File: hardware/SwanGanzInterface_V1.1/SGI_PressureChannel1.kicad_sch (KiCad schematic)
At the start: 18 parts, among them J5 Conn_01x04_Pin, U10 INA122D, U11 OPA2350

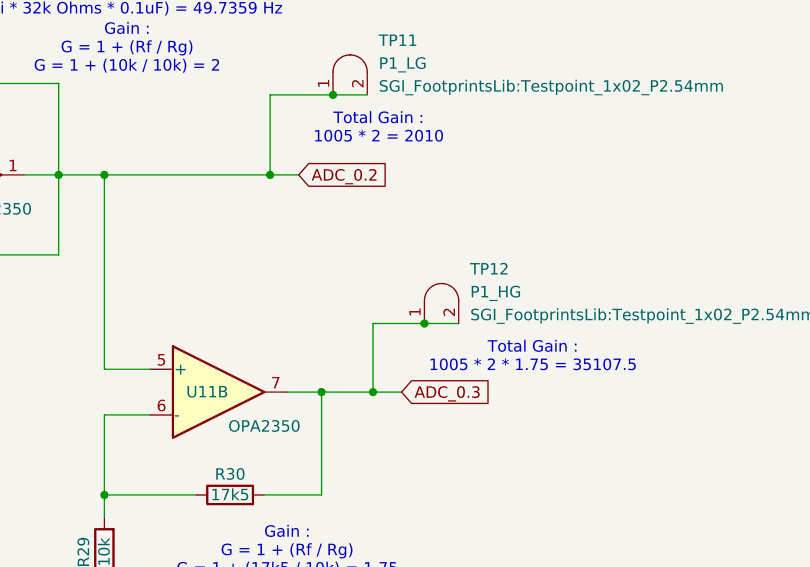
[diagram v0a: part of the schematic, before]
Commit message: Pin Allocation, updated schematic with new pins, reassigned
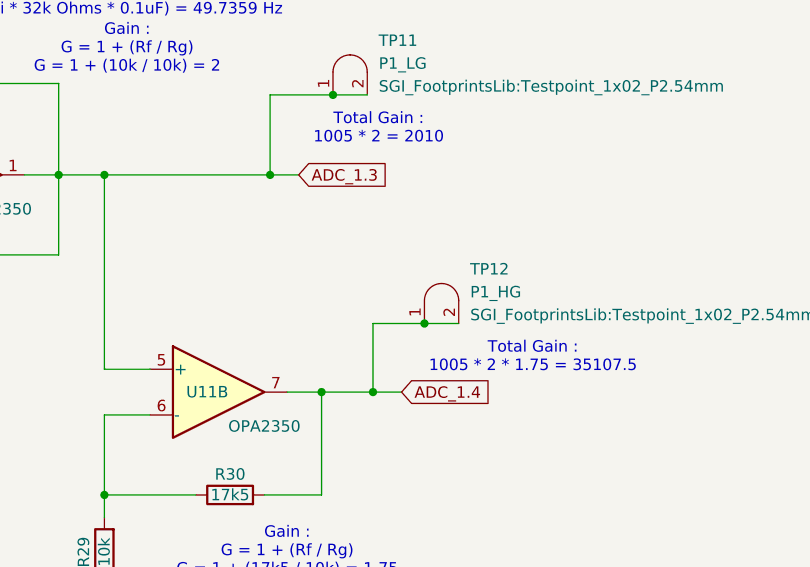
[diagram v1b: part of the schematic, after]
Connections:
- net ADC_0.2 renamed ADC_1.3
- net ADC_0.3 renamed ADC_1.4
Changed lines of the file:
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@@
 		)
 	)
-	(global_label "ADC_0.3"
+	(global_label "ADC_1.4"
 		(shape input)
 		(at 179.07 88.9 0)
@@
 		)
 	)
-	(global_label "ADC_0.2"
+	(global_label "ADC_1.3"
 		(shape input)
 		(at 167.64 64.77 0)

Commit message: Hooked up MSP
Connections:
- net ADC_1.3 renamed P1_LG_ADC_1.3
- net ADC_1.4 renamed P1_HG_ADC_1.4
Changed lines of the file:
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@@
 		)
 	)
-	(global_label "ADC_1.4"
+	(global_label "P1_HG_ADC_1.4"
 		(shape input)
 		(at 179.07 88.9 0)
@@
 		)
 		(property "Intersheetrefs" "${INTERSHEET_REFS}"
-			(at 189.6752 88.9 0)
+			(at 196.6904 88.9 0)
 			(effects
 				(font
@@
 		)
 	)
-	(global_label "ADC_1.3"
+	(global_label "P1_LG_ADC_1.3"
 		(shape input)
 		(at 167.64 64.77 0)
@@
 		)
 		(property "Intersheetrefs" "${INTERSHEET_REFS}"
-			(at 178.2452 64.77 0)
+			(at 184.958 64.77 0)
 			(effects
 				(font

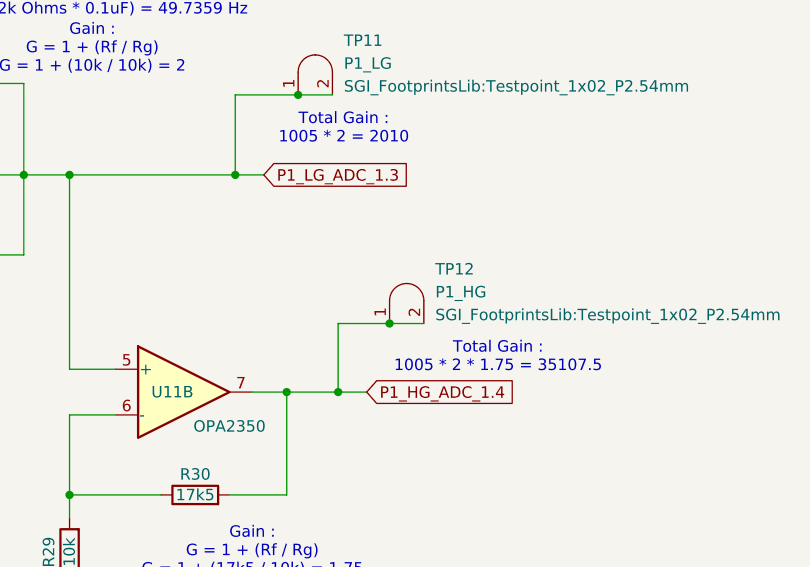
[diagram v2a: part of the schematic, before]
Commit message: Started converting things to use touch screen chip
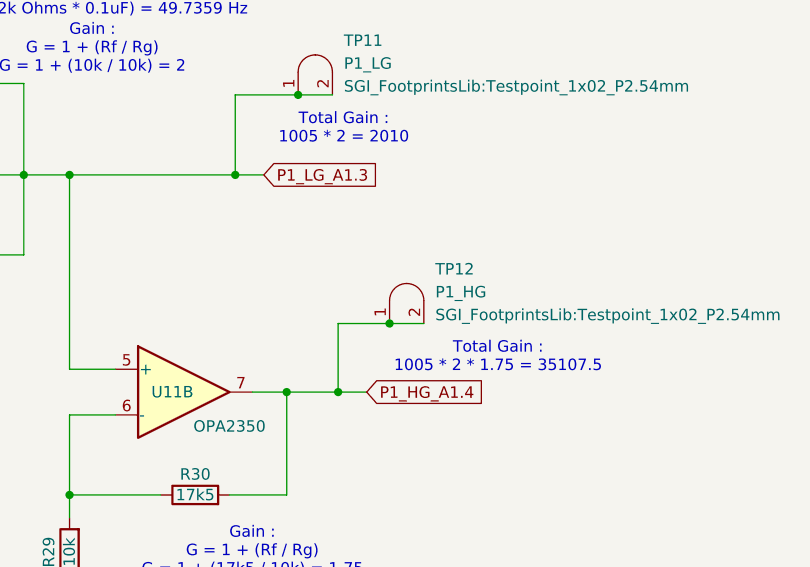
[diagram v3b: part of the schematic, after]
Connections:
- net P1_HG_ADC_1.4 renamed P1_HG_A1.4
- net P1_LG_ADC_1.3 renamed P1_LG_A1.3
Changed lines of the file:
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@@
 		)
 	)
-	(global_label "P1_HG_ADC_1.4"
+	(global_label "P1_HG_A1.4"
 		(shape input)
 		(at 179.07 88.9 0)
@@
 		)
 		(property "Intersheetrefs" "${INTERSHEET_REFS}"
-			(at 196.6904 88.9 0)
+			(at 193.1828 88.9 0)
 			(effects
 				(font
@@
 		)
 	)
-	(global_label "P1_LG_ADC_1.3"
+	(global_label "P1_LG_A1.3"
 		(shape input)
 		(at 167.64 64.77 0)
@@
 		)
 		(property "Intersheetrefs" "${INTERSHEET_REFS}"
-			(at 184.958 64.77 0)
+			(at 181.4504 64.77 0)
 			(effects
 				(font

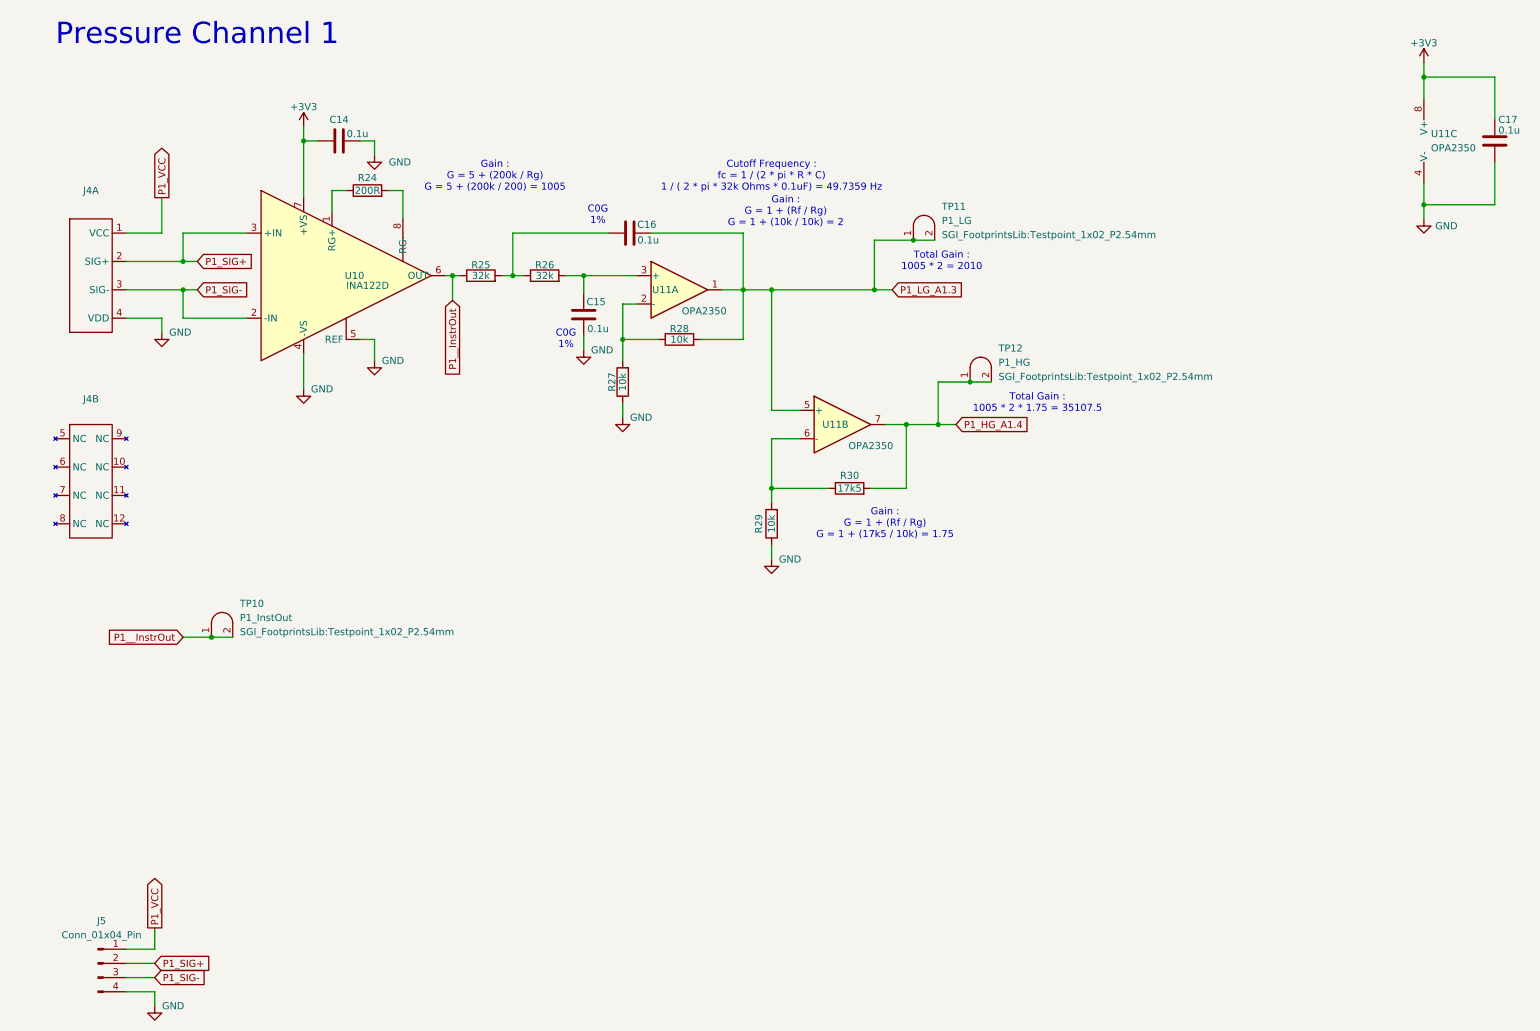
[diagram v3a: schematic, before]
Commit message: Got 64 pin MSP symbol and footprint and started implementation
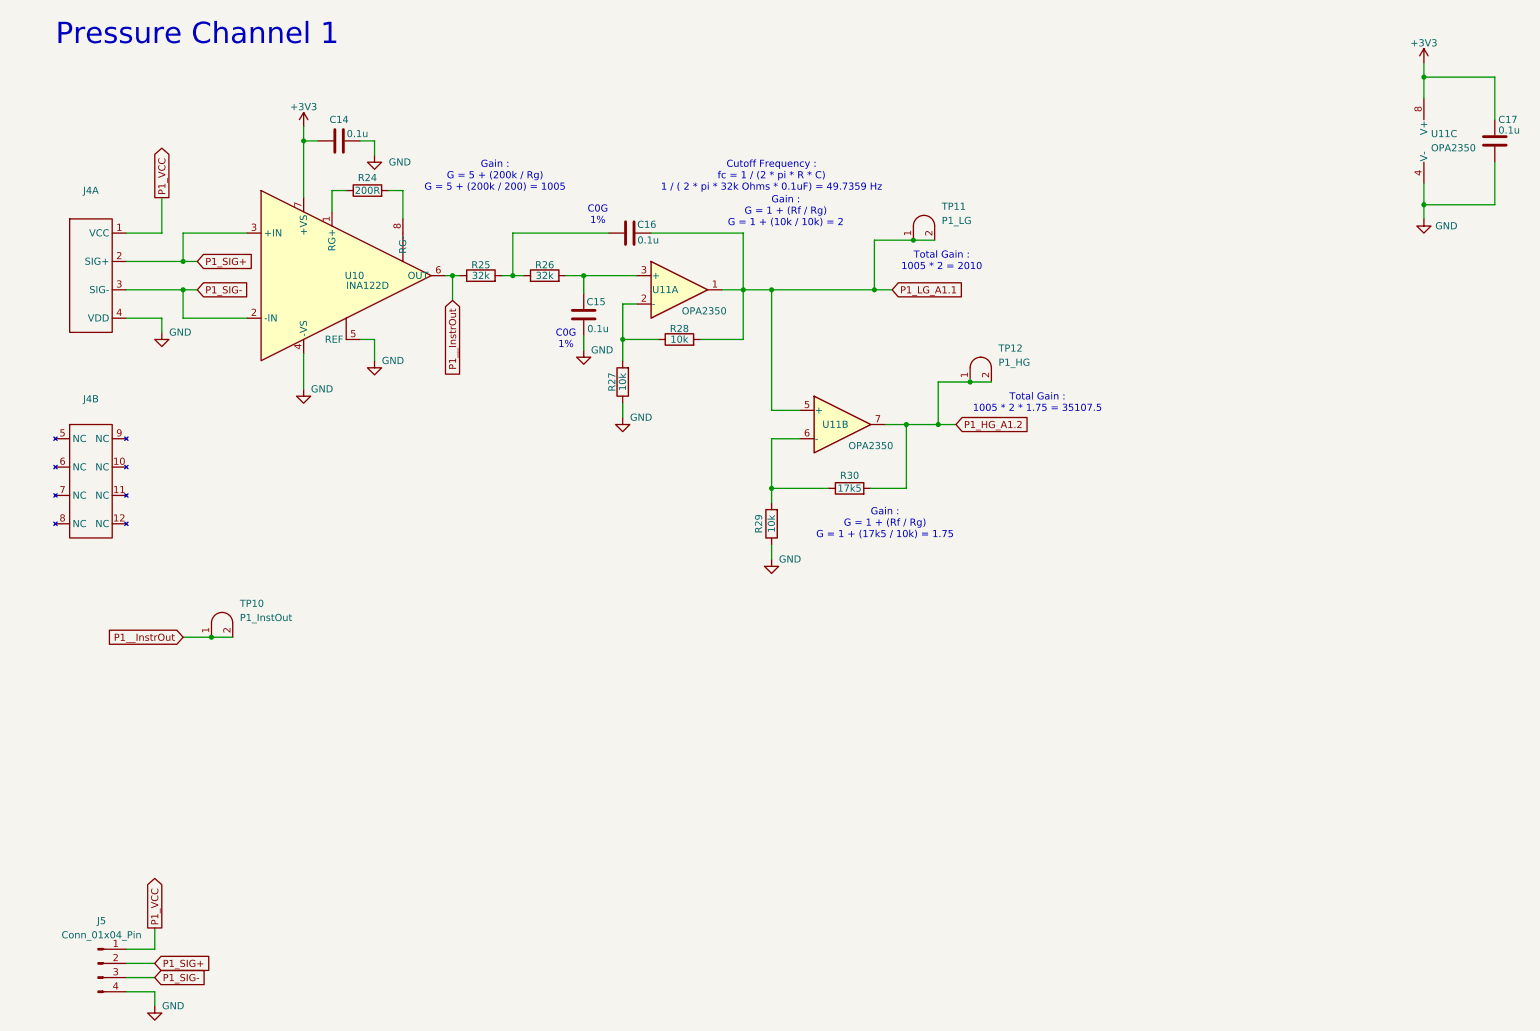
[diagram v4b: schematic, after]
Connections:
- net P1_HG_A1.4 renamed P1_HG_A1.2
- net P1_LG_A1.3 renamed P1_LG_A1.1
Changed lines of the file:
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@@
 		)
 	)
-	(global_label "P1_HG_A1.4"
+	(global_label "P1_HG_A1.2"
 		(shape input)
 		(at 179.07 88.9 0)
@@
 		)
 	)
-	(global_label "P1_LG_A1.3"
+	(global_label "P1_LG_A1.1"
 		(shape input)
 		(at 167.64 64.77 0)
@@
 				)
 				(justify left)
+				(hide yes)
 			)
 		)
@@
 				)
 				(justify left)
+				(hide yes)
 			)
 		)
@@
 				)
 				(justify left)
-			)
-		)
+				(hide yes)
+			)
+		)

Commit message: Schematic Check
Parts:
- renumbered C14 to C19, C15 to C20, C16 to C21, C17 to C22, R24 to R22, R25 to R23, R26 to R24, R27 to R25, R28 to R26, R29 to R27, R30 to R28, U10 to U7, U11 to U8
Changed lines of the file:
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@@
 		(on_board yes)
 		(dnp no)
-		(property "Reference" "#PWR056"
+		(property "Reference" "#PWR054"
 			(at 146.05 119.38 0)
 			(effects
@@
 			(project "SwanGanzInterface"
 				(path "/4e9a6e30-f660-472b-9696-bea1f34b4545/3d8fa9e7-4833-4941-a955-d778effe3e32"
-					(reference "#PWR056")
+					(reference "#PWR054")
 					(unit 1)
 				)
@@
 		(dnp no)
 		(fields_autoplaced yes)
-		(property "Reference" "#PWR052"
+		(property "Reference" "#PWR050"
 			(at 74.93 46.99 0)
 			(effects
@@
 			(project "SwanGanzInterface"
 				(path "/4e9a6e30-f660-472b-9696-bea1f34b4545/3d8fa9e7-4833-4941-a955-d778effe3e32"
-					(reference "#PWR052")
+					(reference "#PWR050")
 					(unit 1)
 				)
@@
 		(on_board yes)
 		(dnp no)
-		(property "Reference" "R28"
+		(property "Reference" "R26"
 			(at 129.54 71.755 90)
 			(effects
@@
 			(project "SwanGanzInterface"
 				(path "/4e9a6e30-f660-472b-9696-bea1f34b4545/3d8fa9e7-4833-4941-a955-d778effe3e32"
-					(reference "R28")
+					(reference "R26")
 					(unit 1)
 				)
@@
 		(on_board yes)
 		(dnp no)
-		(property "Reference" "C15"
+		(property "Reference" "C20"
 			(at 112.903 66.929 0)
 			(effects
@@
 			(project "SwanGanzInterface"
 				(path "/4e9a6e30-f660-472b-9696-bea1f34b4545/3d8fa9e7-4833-4941-a955-d778effe3e32"
-					(reference "C15")
+					(reference "C20")
 					(unit 1)
 				)
@@
 		(on_board yes)
 		(dnp no)
-		(property "Reference" "#PWR054"
+		(property "Reference" "#PWR052"
 			(at 112.395 81.915 0)
 			(effects
@@
 			(project "SwanGanzInterface"
 				(path "/4e9a6e30-f660-472b-9696-bea1f34b4545/3d8fa9e7-4833-4941-a955-d778effe3e32"
-					(reference "#PWR054")
+					(reference "#PWR052")
 					(unit 1)
 				)
@@
 		(on_board yes)
 		(dnp no)
-		(property "Reference" "R26"
+		(property "Reference" "R24"
 			(at 105.41 60.325 90)
 			(effects
@@
 			(project "SwanGanzInterface"
 				(path "/4e9a6e30-f660-472b-9696-bea1f34b4545/3d8fa9e7-4833-4941-a955-d778effe3e32"
-					(reference "R26")
+					(reference "R24")
 					(unit 1)
 				)
@@
 		(on_board yes)
 		(dnp no)
-		(property "Reference" "U11"
+		(property "Reference" "U8"
 			(at 127 64.77 0)
 			(effects
@@
 			(project "SwanGanzInterface"
 				(path "/4e9a6e30-f660-472b-9696-bea1f34b4545/3d8fa9e7-4833-4941-a955-d778effe3e32"
-					(reference "U11")
+					(reference "U8")
 					(unit 1)
 				)
@@
 		(on_board yes)
 		(dnp no)
-		(property "Reference" "#PWR051"
+		(property "Reference" "#PWR049"
 			(at 62.23 88.9 0)
 			(effects
@@
 			(project "SwanGanzInterface"
 				(path "/4e9a6e30-f660-472b-9696-bea1f34b4545/3d8fa9e7-4833-4941-a955-d778effe3e32"
-					(reference "#PWR051")
+					(reference "#PWR049")
 					(unit 1)
 				)
@@
 		(on_board yes)
 		(dnp no)
-		(property "Reference" "#PWR048"
+		(property "Reference" "#PWR046"
 			(at 35.56 199.39 0)
 			(effects
@@
 			(project "SwanGanzInterface"
 				(path "/4e9a6e30-f660-472b-9696-bea1f34b4545/3d8fa9e7-4833-4941-a955-d778effe3e32"
-					(reference "#PWR048")
+					(reference "#PWR046")
 					(unit 1)
 				)
@@
 		(on_board yes)
 		(dnp no)
-		(property "Reference" "#PWR055"
+		(property "Reference" "#PWR053"
 			(at 119.38 93.98 0)
 			(effects
@@
 			(project "SwanGanzInterface"
 				(path "/4e9a6e30-f660-472b-9696-bea1f34b4545/3d8fa9e7-4833-4941-a955-d778effe3e32"
-					(reference "#PWR055")
+					(reference "#PWR053")
 					(unit 1)
 				)
@@
 		(dnp no)
 		(fields_autoplaced yes)
-		(property "Reference" "U11"
+		(property "Reference" "U8"
 			(at 264.16 36.8299 0)
 			(effects
@@
 			(project "SwanGanzInterface"
 				(path "/4e9a6e30-f660-472b-9696-bea1f34b4545/3d8fa9e7-4833-4941-a955-d778effe3e32"
-					(reference "U11")
+					(reference "U8")
 					(unit 3)
 				)
@@
 		(dnp no)
 		(fields_autoplaced yes)
-		(property "Reference" "#PWR058"
+		(property "Reference" "#PWR056"
 			(at 262.89 58.42 0)
 			(effects
@@
 			(project "SwanGanzInterface"
 				(path "/4e9a6e30-f660-472b-9696-bea1f34b4545/3d8fa9e7-4833-4941-a955-d778effe3e32"
-					(reference "#PWR058")
+					(reference "#PWR056")
 					(unit 1)
 				)
@@
 		(on_board yes)
 		(dnp no)
-		(property "Reference" "#PWR050"
+		(property "Reference" "#PWR048"
 			(at 62.23 39.37 0)
 			(effects
@@
 			(project "SwanGanzInterface"
 				(path "/4e9a6e30-f660-472b-9696-bea1f34b4545/3d8fa9e7-4833-4941-a955-d778effe3e32"
-					(reference "#PWR050")
+					(reference "#PWR048")
 					(unit 1)
 				)
@@
 		(on_board yes)
 		(dnp no)
-		(property "Reference" "R29"
+		(property "Reference" "R27"
 			(at 143.764 106.68 90)
 			(effects
@@
 			(project "SwanGanzInterface"
 				(path "/4e9a6e30-f660-472b-9696-bea1f34b4545/3d8fa9e7-4833-4941-a955-d778effe3e32"
-					(reference "R29")
+					(reference "R27")
 					(unit 1)
 				)
@@
 		(on_board yes)
 		(dnp no)
-		(property "Reference" "U11"
+		(property "Reference" "U8"
 			(at 157.48 88.9 0)
 			(effects
@@
 			(project "SwanGanzInterface"
 				(path "/4e9a6e30-f660-472b-9696-bea1f34b4545/3d8fa9e7-4833-4941-a955-d778effe3e32"
-					(reference "U11")
+					(reference "U8")
 					(unit 2)
 				)
@@
 		(on_board yes)
 		(dnp no)
-		(property "Reference" "#PWR049"
+		(property "Reference" "#PWR047"
 			(at 36.83 78.74 0)
 			(effects
@@
 			(project "SwanGanzInterface"
 				(path "/4e9a6e30-f660-472b-9696-bea1f34b4545/3d8fa9e7-4833-4941-a955-d778effe3e32"
-					(reference "#PWR049")
+					(reference "#PWR047")
 					(unit 1)
 				)
@@
 		(on_board yes)
 		(dnp no)
-		(property "Reference" "U10"
+		(property "Reference" "U7"
 			(at 69.596 62.23 0)
 			(effects
@@
 			(project "SwanGanzInterface"
 				(path "/4e9a6e30-f660-472b-9696-bea1f34b4545/3d8fa9e7-4833-4941-a955-d778effe3e32"
-					(reference "U10")
+					(reference "U7")
 					(unit 1)
 				)
@@
 		(on_board yes)
 		(dnp no)
-		(property "Reference" "R24"
+		(property "Reference" "R22"
 			(at 73.66 44.704 90)
 			(effects
@@
 			(project "SwanGanzInterface"
 				(path "/4e9a6e30-f660-472b-9696-bea1f34b4545/3d8fa9e7-4833-4941-a955-d778effe3e32"
-					(reference "R24")
+					(reference "R22")
 					(unit 1)
 				)
@@
 		(on_board yes)
 		(dnp no)
-		(property "Reference" "#PWR053"
+		(property "Reference" "#PWR051"
 			(at 74.93 83.82 0)
 			(effects
@@
 			(project "SwanGanzInterface"
 				(path "/4e9a6e30-f660-472b-9696-bea1f34b4545/3d8fa9e7-4833-4941-a955-d778effe3e32"
-					(reference "#PWR053")
+					(reference "#PWR051")
 					(unit 1)
 				)
@@
 		(on_board yes)
 		(dnp no)
-		(property "Reference" "R30"
+		(property "Reference" "R28"
 			(at 160.02 98.044 90)
 			(effects
@@
 			(project ""
 				(path "/4e9a6e30-f660-472b-9696-bea1f34b4545/3d8fa9e7-4833-4941-a955-d778effe3e32"
-					(reference "R30")
+					(reference "R28")
 					(unit 1)
 				)
@@
 		(on_board yes)
 		(dnp no)
-		(property "Reference" "C17"
+		(property "Reference" "C22"
 			(at 276.225 34.29 0)
 			(effects
@@
 			(project "SwanGanzInterface"
 				(path "/4e9a6e30-f660-472b-9696-bea1f34b4545/3d8fa9e7-4833-4941-a955-d778effe3e32"
-					(reference "C17")
+					(reference "C22")
 					(unit 1)
 				)
@@
 		(on_board yes)
 		(dnp no)
-		(property "Reference" "R27"
+		(property "Reference" "R25"
 			(at 117.475 81.28 90)
 			(effects
@@
 			(project "SwanGanzInterface"
 				(path "/4e9a6e30-f660-472b-9696-bea1f34b4545/3d8fa9e7-4833-4941-a955-d778effe3e32"
-					(reference "R27")
+					(reference "R25")
 					(unit 1)
 				)
@@
 		(on_board yes)
 		(dnp no)
-		(property "Reference" "C14"
+		(property "Reference" "C19"
 			(at 68.58 34.29 90)
 			(effects
@@
 			(project "SwanGanzInterface"
 				(path "/4e9a6e30-f660-472b-9696-bea1f34b4545/3d8fa9e7-4833-4941-a955-d778effe3e32"
-					(reference "C14")
+					(reference "C19")
 					(unit 1)
 				)
@@
 		(on_board yes)
 		(dnp no)
-		(property "Reference" "R25"
+		(property "Reference" "R23"
 			(at 93.98 60.325 90)
 			(effects
@@
 			(project "SwanGanzInterface"
 				(path "/4e9a6e30-f660-472b-9696-bea1f34b4545/3d8fa9e7-4833-4941-a955-d778effe3e32"
-					(reference "R25")
+					(reference "R23")
 					(unit 1)
 				)
@@
 		(on_board yes)
 		(dnp no)
-		(property "Reference" "C16"
+		(property "Reference" "C21"
 			(at 123.698 53.086 90)
 			(effects
@@
 			(project "SwanGanzInterface"
 				(path "/4e9a6e30-f660-472b-9696-bea1f34b4545/3d8fa9e7-4833-4941-a955-d778effe3e32"
-					(reference "C16")
+					(reference "C21")
 					(unit 1)
 				)
@@
 		(on_board yes)
 		(dnp no)
-		(property "Reference" "#PWR057"
+		(property "Reference" "#PWR055"
 			(at 262.89 27.94 0)
 			(effects
@@
 			(project "SwanGanzInterface"
 				(path "/4e9a6e30-f660-472b-9696-bea1f34b4545/3d8fa9e7-4833-4941-a955-d778effe3e32"
-					(reference "#PWR057")
-					(unit 1)
-				)
+					(reference "#PWR055")
+					(unit 1)
+				)

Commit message: Filter paramaters and assigned footprints
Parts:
- C20, C21: value 0.1u -> 0.022u; footprint Capacitor_SMD:C_1206_3216Metric -> Capacitor_SMD:C_0603_1608Metric
- R23, R24: value 32k -> 100k
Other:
- note added: "Cutoff Frequency : fc = 1 / (2 * pi * R * C) 1 / ( 2 * pi * 100k Ohms * 0.022uF) = 74.3432 Hz"
- note removed: "Cutoff Frequency : fc = 1 / (2 * pi * R * C) 1 / ( 2 * pi * 32k Ohms * 0.1uF) = 49.7359 Hz"
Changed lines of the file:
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@@
 		)
 	)
-	(text "Cutoff Frequency :\nfc = 1 / (2 * pi * R * C)\n1 / ( 2 * pi * 32k Ohms * 0.1uF) = 49.7359 Hz"
+	(text "Cutoff Frequency :\nfc = 1 / (2 * pi * R * C)\n1 / ( 2 * pi * 100k Ohms * 0.022uF) = 74.3432 Hz"
 		(exclude_from_sim no)
 		(at 146.05 44.45 0)
@@
 			)
 		)
-		(property "Value" "0.1u"
+		(property "Value" "0.022u"
 			(at 113.03 71.755 0)
 			(effects
@@
 			)
 		)
-		(property "Footprint" "Capacitor_SMD:C_1206_3216Metric"
+		(property "Footprint" "Capacitor_SMD:C_0603_1608Metric"
 			(at 113.3602 73.025 0)
 			(effects
@@
 			)
 		)
-		(property "Value" "32k"
+		(property "Value" "100k"
 			(at 105.41 62.23 90)
 			(effects
@@
 			)
 		)
-		(property "Value" "32k"
+		(property "Value" "100k"
 			(at 93.98 62.23 90)
 			(effects
@@
 			)
 		)
-		(property "Value" "0.1u"
-			(at 123.952 55.88 90)
+		(property "Value" "0.022u"
+			(at 124.714 55.88 90)
 			(effects
 				(font
@@
 			)
 		)
-		(property "Footprint" "Capacitor_SMD:C_1206_3216Metric"
+		(property "Footprint" "Capacitor_SMD:C_0603_1608Metric"
 			(at 124.46 53.6448 0)
 			(effects
